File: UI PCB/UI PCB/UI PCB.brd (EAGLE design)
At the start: 67.3 x 50.5 mm, 23 parts, among them IC1 MCP23S17SP, IC2 MCP23S17SP, X1 JST-XH-02-PIN-ROUND-PAD, X2 JST-XH-02-PIN-ROUND-PAD, X3 JST-XH-02-PIN-ROUND-PAD, X4 JST-XH-02-PIN-ROUND-PAD, X5 JST-XH-05-PIN-ROUND-PAD, X6 JST-XH-05-PIN-ROUND-PAD, X7 JST-XH-05-PIN-ROUND-PAD, X8 JST-XH-05-PIN-ROUND-PAD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

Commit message: gerber files toegevoegd
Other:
- board size 67.3 x 50.5 mm -> 67.3 x 50.2 mm
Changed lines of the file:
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@@
 <?xml version="1.0" encoding="utf-8"?>
 <!DOCTYPE eagle SYSTEM "eagle.dtd">
-<eagle version="9.5.1">
+<eagle version="9.5.2">
 <drawing>
 <settings>
@@
 <board>
 <plain>
-<wire x1="0" y1="0" x2="67.29" y2="0" width="0" layer="20"/>
-<wire x1="67.29" y1="0" x2="67.29" y2="50.47" width="0" layer="20"/>
-<wire x1="67.29" y1="50.47" x2="0" y2="50.47" width="0" layer="20"/>
-<wire x1="0" y1="50.47" x2="0" y2="0" width="0" layer="20"/>
+<wire x1="0" y1="0" x2="67.31" y2="0" width="0" layer="20"/>
+<wire x1="67.31" y1="0" x2="67.31" y2="50.165" width="0" layer="20"/>
+<wire x1="67.31" y1="50.165" x2="0" y2="50.165" width="0" layer="20"/>
+<wire x1="0" y1="50.165" x2="0" y2="0" width="0" layer="20"/>
 <hole x="9.652" y="36.068" drill="3.2"/>
 <hole x="49.53" y="36.068" drill="3.2"/>
 <hole x="49.53" y="8.128" drill="3.2"/>
 <text x="8.636" y="49.022" size="1.016" layer="25">Synth Module UI V1.0 - Brian Oehlers, Ruben van Renswoude, Julian Schotborgh</text>
-<dimension x1="43.18" y1="36.83" x2="43.18" y2="34.29" x3="69.215" y3="35.56" textsize="1.778" layer="1"/>
-<dimension x1="43.18" y1="34.29" x2="43.18" y2="31.75" x3="73.025" y3="33.02" textsize="1.778" layer="1"/>
-<dimension x1="43.18" y1="29.21" x2="43.18" y2="31.75" x3="76.835" y3="30.48" textsize="1.778" layer="1"/>
-<dimension x1="43.18" y1="29.21" x2="43.18" y2="26.67" x3="82.55" y3="27.94" textsize="1.778" layer="1"/>
-<dimension x1="43.18" y1="3.81" x2="43.18" y2="36.83" x3="92.71" y3="20.32" textsize="1.778" layer="1"/>
-<dimension x1="43.18" y1="24.13" x2="43.18" y2="26.67" x3="79.375" y3="25.4" textsize="1.778" layer="1"/>
 <dimension x1="67.29" y1="50.47" x2="0" y2="50.47" x3="33.645" y3="54.61" textsize="1.778" layer="1"/>
 </plain>

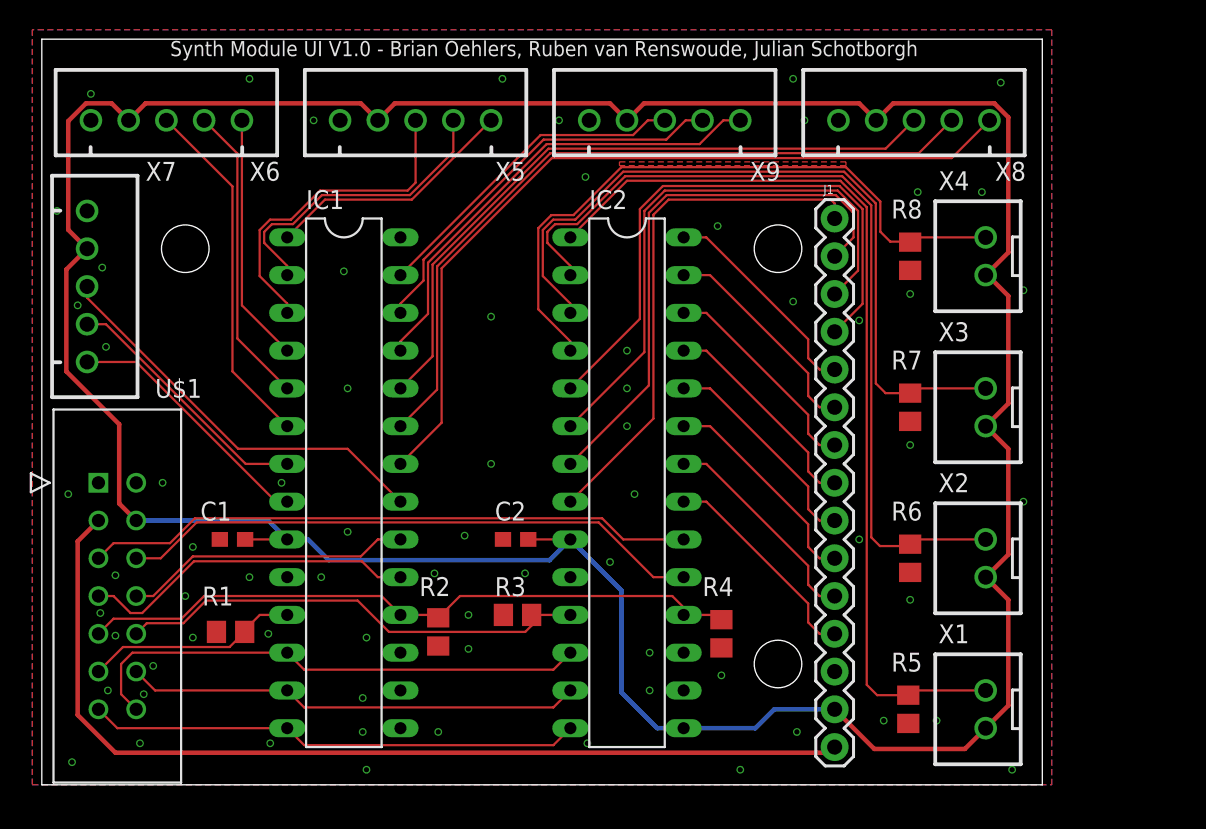
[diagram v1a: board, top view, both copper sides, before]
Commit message: nieuwe gerber files toegevoegd
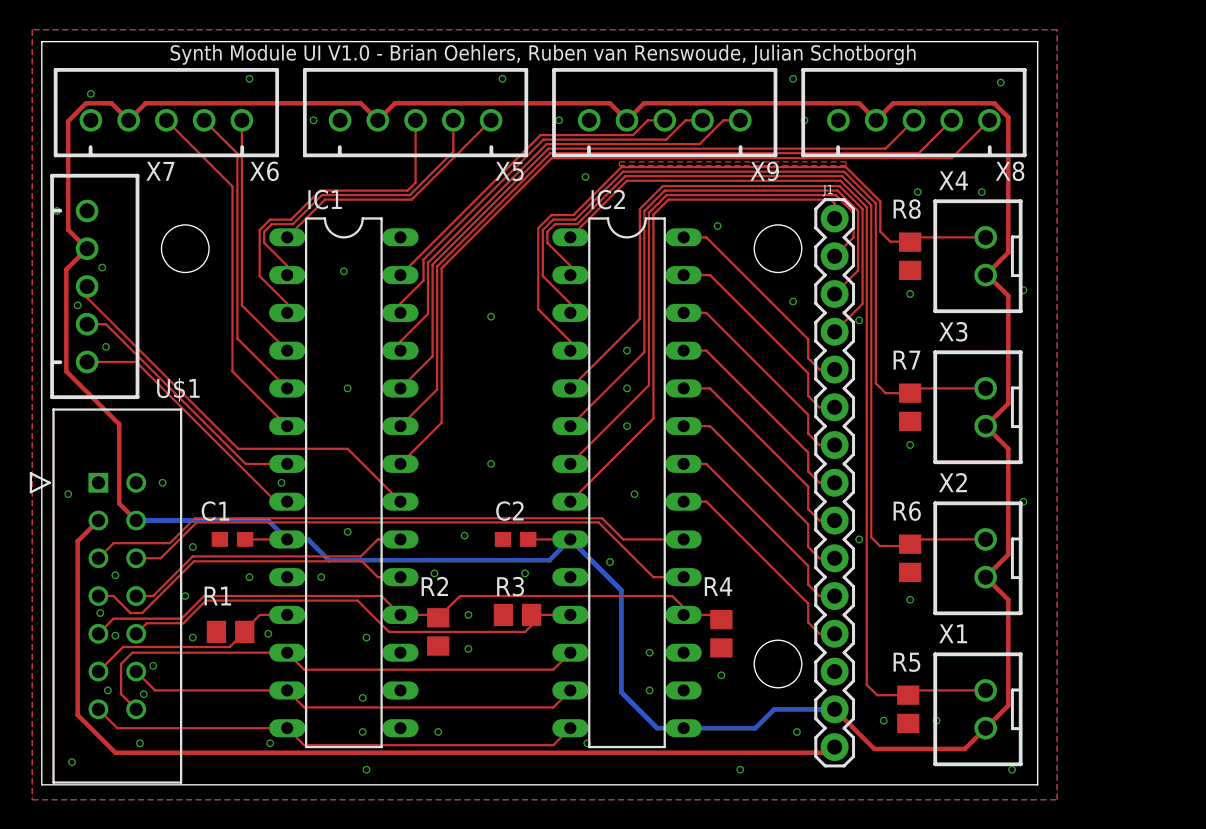
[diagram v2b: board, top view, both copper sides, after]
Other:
- board size 67.3 x 50.2 mm -> 67 x 50 mm
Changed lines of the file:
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@@
 <setting verticaltext="up"/>
 </settings>
-<grid distance="25" unitdist="mil" unit="mil" style="lines" multiple="1" display="yes" altdistance="5" altunitdist="mil" altunit="mil"/>
+<grid distance="0.003125" unitdist="mic" unit="mm" style="lines" multiple="1" display="yes" altdistance="5" altunitdist="mil" altunit="mil"/>
 <layers>
 <layer number="1" name="Top" color="4" fill="1" visible="yes" active="yes"/>
@@
 <board>
 <plain>
-<wire x1="0" y1="0" x2="67.31" y2="0" width="0" layer="20"/>
-<wire x1="67.31" y1="0" x2="67.31" y2="50.165" width="0" layer="20"/>
-<wire x1="67.31" y1="50.165" x2="0" y2="50.165" width="0" layer="20"/>
-<wire x1="0" y1="50.165" x2="0" y2="0" width="0" layer="20"/>
+<wire x1="0" y1="0" x2="67" y2="0" width="0" layer="20"/>
+<wire x1="67" y1="0" x2="67" y2="50" width="0" layer="20"/>
+<wire x1="67" y1="50" x2="0" y2="50" width="0" layer="20"/>
+<wire x1="0" y1="50" x2="0" y2="0" width="0" layer="20"/>
 <hole x="9.652" y="36.068" drill="3.2"/>
 <hole x="49.53" y="36.068" drill="3.2"/>
 <hole x="49.53" y="8.128" drill="3.2"/>
-<text x="8.636" y="49.022" size="1.016" layer="25">Synth Module UI V1.0 - Brian Oehlers, Ruben van Renswoude, Julian Schotborgh</text>
-<dimension x1="67.29" y1="50.47" x2="0" y2="50.47" x3="33.645" y3="54.61" textsize="1.778" layer="1"/>
+<text x="8.5877875" y="48.7326625" size="1.016" layer="25">Synth Module UI V1.0 - Brian Oehlers, Ruben van Renswoude, Julian Schotborgh</text>
+<dimension x1="66.98" y1="50.67" x2="0" y2="50.47" x3="33.4776375" y3="54.70998125" textsize="1.778" layer="1"/>
 </plain>
 <attributes>
@@
 <polygon width="0.1524" layer="1">
 <vertex x="-0.635" y="50.8"/>
-<vertex x="-0.635" y="0"/>
-<vertex x="67.945" y="0"/>
-<vertex x="67.945" y="50.8"/>
+<vertex x="-0.635" y="-1"/>
+<vertex x="68.31" y="-1"/>
+<vertex x="68.31" y="50.8"/>
 </polygon>
 <polygon width="0.1524" layer="16">
 <vertex x="-0.635" y="50.8"/>
-<vertex x="-0.635" y="0"/>
-<vertex x="67.945" y="0"/>
-<vertex x="67.945" y="50.8"/>
+<vertex x="-0.635" y="-1"/>
+<vertex x="68.31" y="-1"/>
+<vertex x="68.31" y="50.8"/>
 </polygon>
 <via x="10.16" y="16.002" extent="1-16" drill="0.35"/>
